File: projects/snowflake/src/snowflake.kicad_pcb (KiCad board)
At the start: 2 copper layers, 170 x 162 mm, 51 parts, among them SW1 SW_Push, U1 XIAO-ESP32-C3-SMD

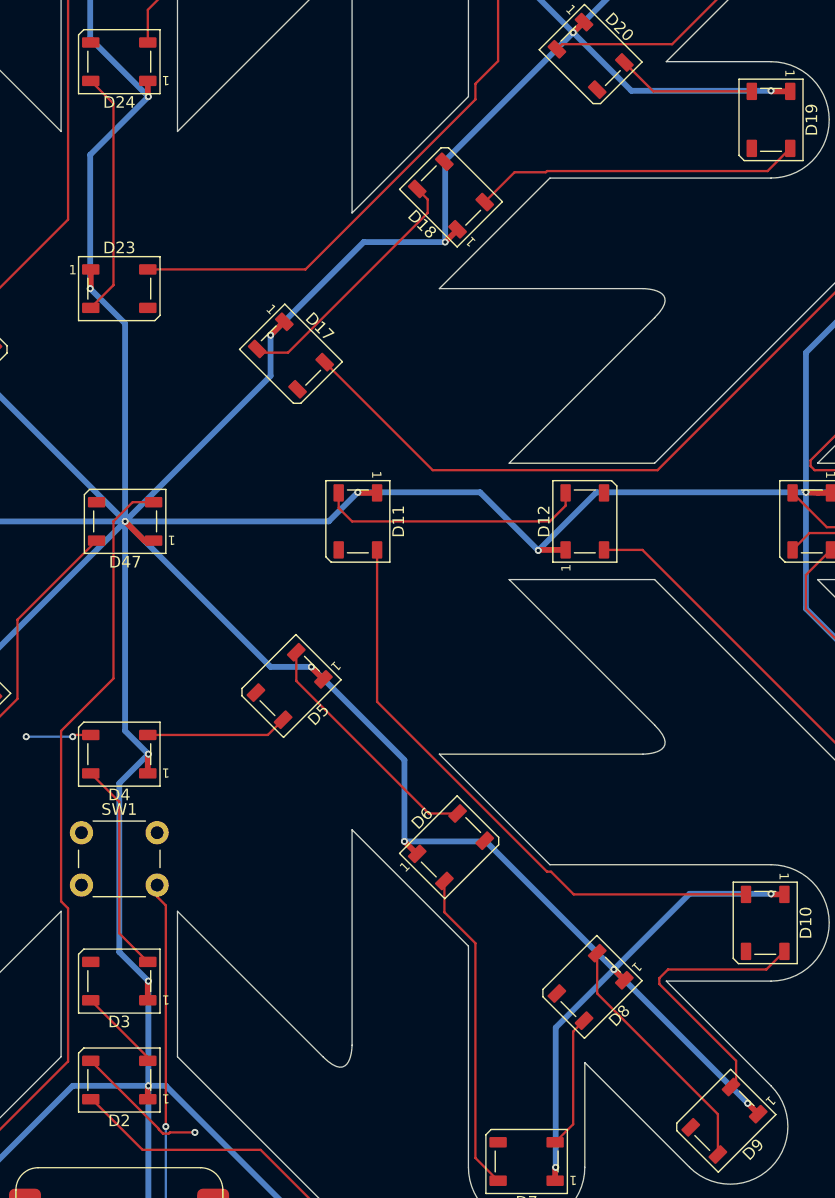
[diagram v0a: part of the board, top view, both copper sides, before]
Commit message: update footprint + dad pcba
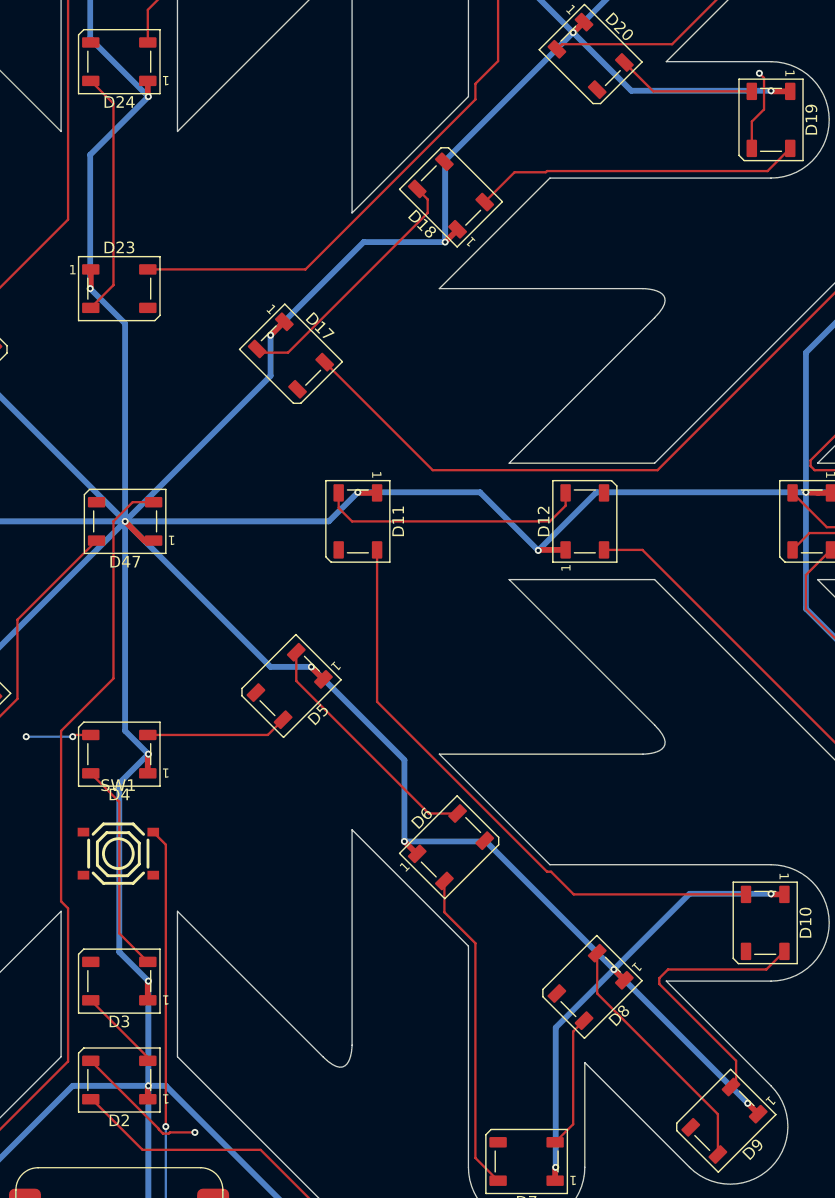
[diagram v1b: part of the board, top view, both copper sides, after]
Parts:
- SW1: footprint Button_Switch_THT:SW_PUSH_6mm -> LCSC:SW-SMD_4P-L5.1-W5.1-P3.70-LS6.5-TL_H1.5
- moved SW1 3.64 mm to (105.9, 130.0)
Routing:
- net GND: track 41.0 -> 48.1 mm, vias 4 -> 5
- net Net-(U1-GPIO4_A2_D2): track 39.2 -> 43.9 mm
